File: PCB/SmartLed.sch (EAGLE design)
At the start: 46 parts, among them IC2 DS1307, IC3 MEGA8-P, K1 G5LE, Q1 32.768khz, T1 BC337

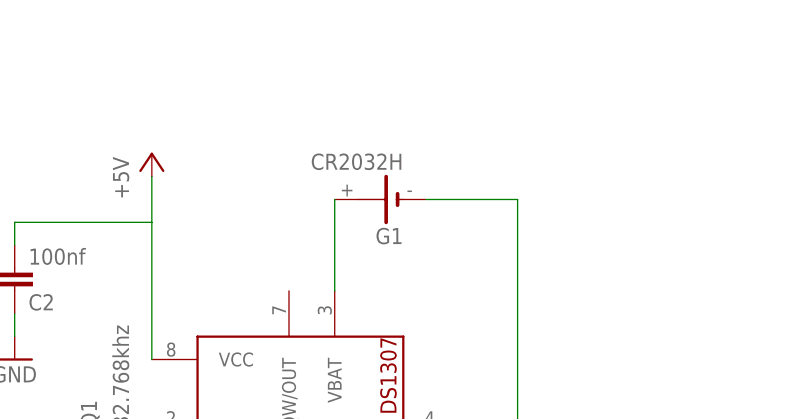
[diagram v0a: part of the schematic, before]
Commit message: Add 100n capacitor beside 3.6v lithium battery & change the battery footprint
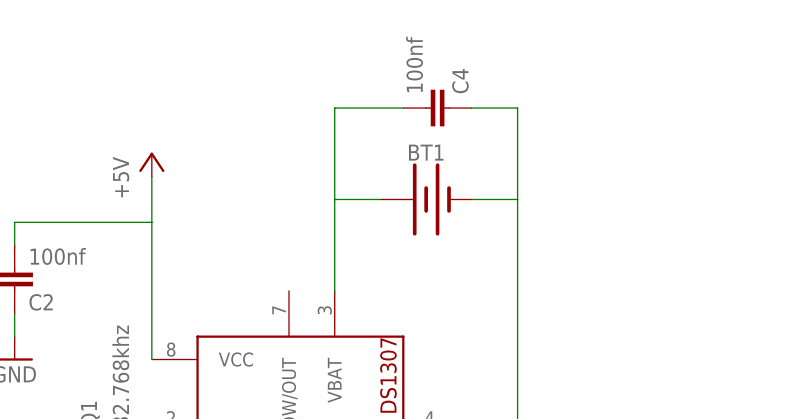
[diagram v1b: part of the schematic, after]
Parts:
- removed G1: CR2032H, battery:CR2032H
- added BT1: (no value), SparkFun-Batteries:BATTERY-20MM_PTH
- added C4: 100nf, rcl:C-EU025-025X050
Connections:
- removed net N$18: G1.+, IC2.VBAT
- new net N$44: BT1.+, C4.2, IC2.VBAT
- net GND: now also BT1.-, C4.1; no longer G1.-
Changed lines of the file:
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@@
 <layer number="112" name="tSilk" color="7" fill="1" visible="no" active="yes"/>
 <layer number="113" name="ReferenceLS" color="7" fill="1" visible="no" active="no"/>
+<layer number="114" name="Badge_Outline" color="7" fill="1" visible="yes" active="yes"/>
+<layer number="115" name="ReferenceISLANDS" color="7" fill="1" visible="yes" active="yes"/>
 <layer number="116" name="Patch_BOT" color="9" fill="4" visible="no" active="yes"/>
 <layer number="118" name="Rect_Pads" color="7" fill="1" visible="no" active="no"/>
@@
 <part name="D1" library="diode" deviceset="1N4148" device="DO35-7"/>
 <part name="IC2" library="adafruit" deviceset="DS1307" device=""/>
-<part name="G1" library="battery" deviceset="CR2032H" device=""/>
 <part name="Q1" library="crystal" deviceset="CRYSTAL" device="HC49U70" value="32.768khz"/>
 <part name="IC3" library="atmel" deviceset="MEGA8-P" device=""/>
@@
 <part name="JP2" library="pinhead" deviceset="PINHD-1X5" device=""/>
 <part name="C1" library="rcl" deviceset="CPOL-EU" device="E2.5-5" value="4.7uf"/>
+<part name="C4" library="rcl" deviceset="C-EU" device="025-025X050" value="100nf"/>
+<part name="BT1" library="SparkFun-Batteries" deviceset="BATTERY" device="-20MM_PTH"/>
 </parts>
 <sheets>
@@
 <instance part="D1" gate="G$1" x="208.28" y="66.04" rot="R90"/>
 <instance part="IC2" gate="G$1" x="208.28" y="157.48" rot="R90"/>
-<instance part="G1" gate="1" x="215.9" y="182.88" rot="R180"/>
 <instance part="Q1" gate="G$1" x="185.42" y="154.94" rot="R90"/>
 <instance part="IC3" gate="G$1" x="66.04" y="88.9"/>
@@
 <instance part="JP2" gate="A" x="101.6" y="116.84"/>
 <instance part="C1" gate="G$1" x="-25.4" y="58.42"/>
+<instance part="C4" gate="G$1" x="223.52" y="193.04" rot="MR90"/>
+<instance part="BT1" gate="G$1" x="220.98" y="182.88"/>
 </instances>
 <busses>
@@
 </segment>
 <segment>
+<pinref part="GND5" gate="1" pin="GND"/>
 <pinref part="IC2" gate="G$1" pin="GND"/>
 <wire x1="223.52" y1="157.48" x2="231.14" y2="157.48" width="0.1524" layer="91"/>
-<pinref part="GND5" gate="1" pin="GND"/>
-<pinref part="G1" gate="1" pin="-"/>
-<wire x1="220.98" y1="182.88" x2="231.14" y2="182.88" width="0.1524" layer="91"/>
+<wire x1="231.14" y1="193.04" x2="231.14" y2="182.88" width="0.1524" layer="91"/>
+<pinref part="C4" gate="G$1" pin="1"/>
 <wire x1="231.14" y1="182.88" x2="231.14" y2="157.48" width="0.1524" layer="91"/>
+<wire x1="226.06" y1="193.04" x2="231.14" y2="193.04" width="0.1524" layer="91"/>
+<pinref part="BT1" gate="G$1" pin="-"/>
+<wire x1="226.06" y1="182.88" x2="231.14" y2="182.88" width="0.1524" layer="91"/>
 </segment>
 <segment>
@@
 </segment>
 </net>
-<net name="N$18" class="0">
-<segment>
-<pinref part="G1" gate="1" pin="+"/>
-<pinref part="IC2" gate="G$1" pin="VBAT"/>
-<wire x1="210.82" y1="182.88" x2="210.82" y2="172.72" width="0.1524" layer="91"/>
-</segment>
-</net>
 <net name="N$21" class="0">
 <segment>
@@
 </segment>
 </net>
+<net name="N$44" class="0">
+<segment>
+<pinref part="C4" gate="G$1" pin="2"/>
+<wire x1="218.44" y1="193.04" x2="210.82" y2="193.04" width="0.1524" layer="91"/>
+<pinref part="IC2" gate="G$1" pin="VBAT"/>
+<wire x1="210.82" y1="193.04" x2="210.82" y2="182.88" width="0.1524" layer="91"/>
+<pinref part="BT1" gate="G$1" pin="+"/>
+<wire x1="210.82" y1="182.88" x2="210.82" y2="172.72" width="0.1524" layer="91"/>
+<wire x1="215.9" y1="182.88" x2="210.82" y2="182.88" width="0.1524" layer="91"/>
+</segment>
+</net>

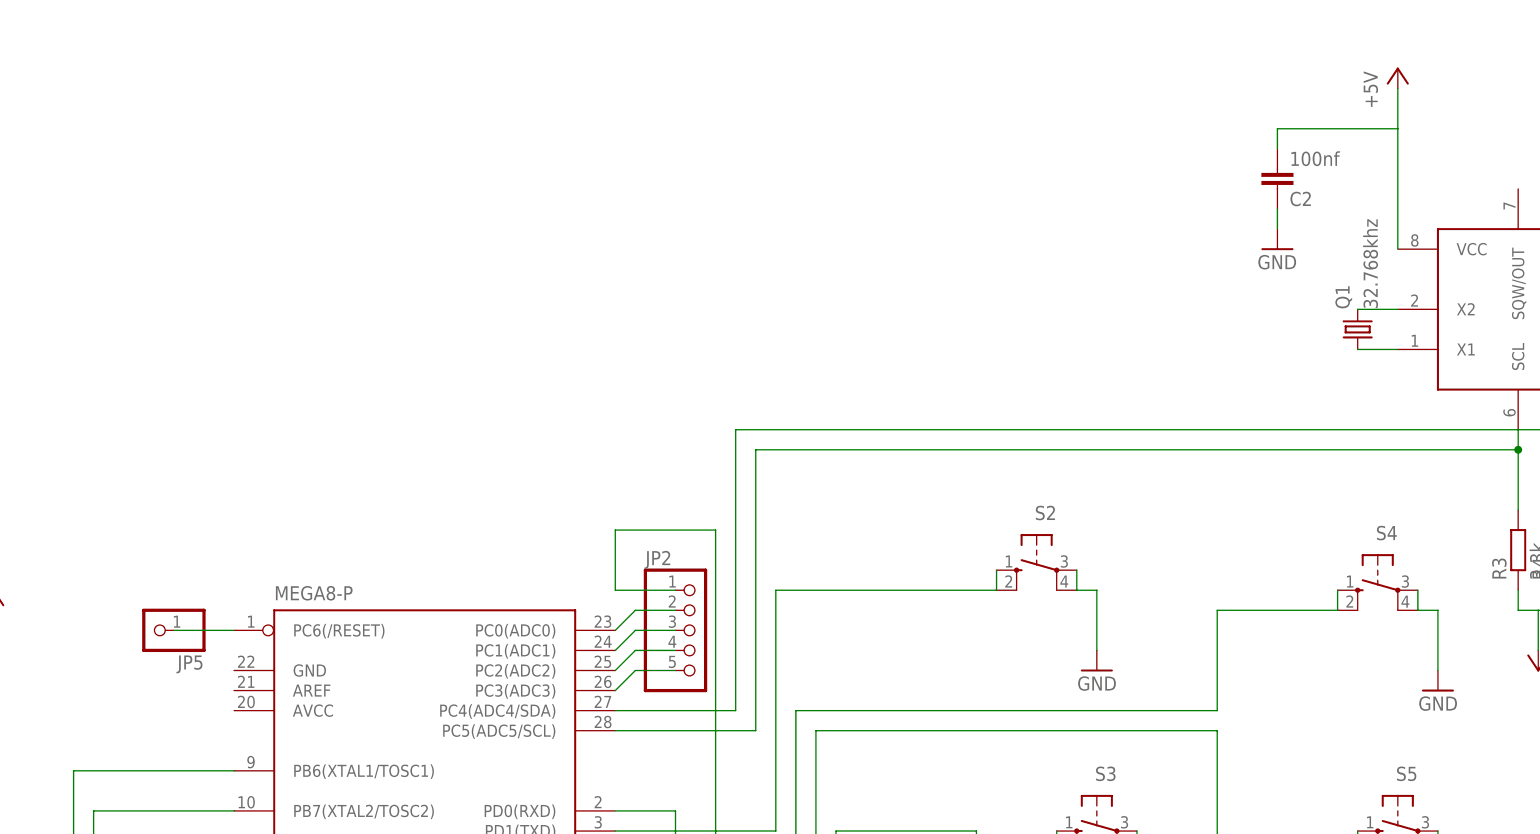
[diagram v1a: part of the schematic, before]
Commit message: Infrared receiver was added & crystal footprint size was corrected
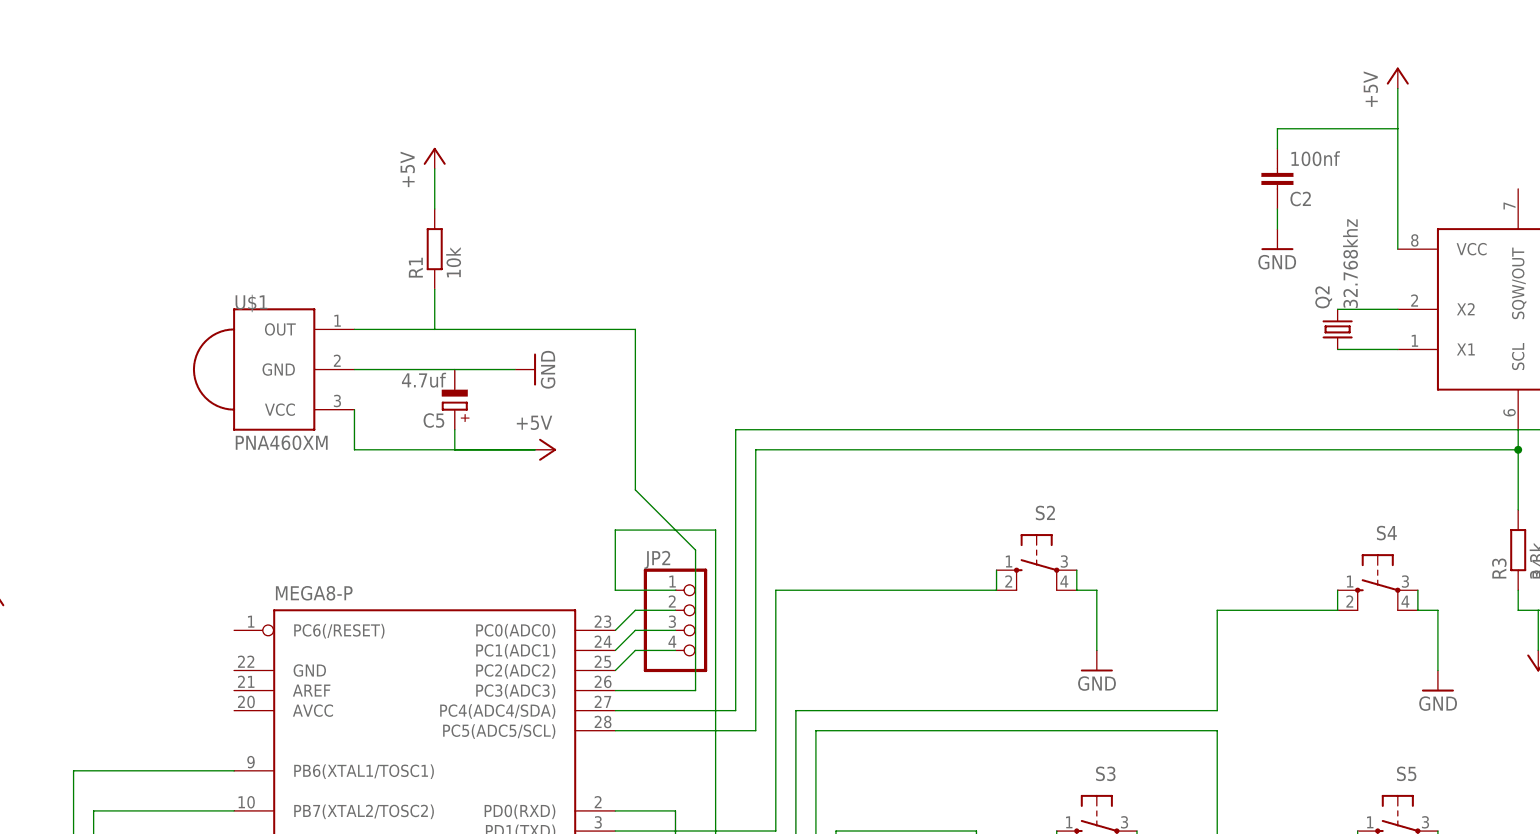
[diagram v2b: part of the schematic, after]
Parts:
- removed JP5: (no value), pinhead:PINHD-1X1
- removed Q1: 32.768khz, crystal:CRYSTALHC49U70
- added C5: 4.7uf, rcl:CPOL-EUE2.5-5
- added Q2: 32.768khz, crystal:CRYSTALTC26V
- added R1: 10k, rcl:R-EU_0207/10
- added U$1: PNA460XM, adafruit:PNA460XM
- JP2: device pinhead:PINHD-1X5 -> pinhead:PINHD-1X4
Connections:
- removed net N$36: IC3.PC3(ADC3), JP2.5
- removed net N$43: IC3.PC6(/RESET), JP5.1
- new net N$46: IC3.PC3(ADC3), R1.1, U$1.OUT
- net +5V: now also C5.+, R1.2, U$1.VCC
- net GND: now also C5.-, U$1.GND
- net N$21: now also Q2.1; no longer Q1.1
- net N$22: now also Q2.2; no longer Q1.2
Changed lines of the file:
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@@
 <part name="D1" library="diode" deviceset="1N4148" device="DO35-7"/>
 <part name="IC2" library="adafruit" deviceset="DS1307" device=""/>
-<part name="Q1" library="crystal" deviceset="CRYSTAL" device="HC49U70" value="32.768khz"/>
 <part name="IC3" library="atmel" deviceset="MEGA8-P" device=""/>
 <part name="B1" library="rectifier" deviceset="RB1A" device=""/>
@@
 <part name="IC4" library="v-reg" deviceset="78XXS" device=""/>
 <part name="GND8" library="supply1" deviceset="GND" device=""/>
-<part name="JP5" library="pinhead" deviceset="PINHD-1X1" device=""/>
 <part name="JP1" library="pinhead" deviceset="PINHD-1X5" device=""/>
-<part name="JP2" library="pinhead" deviceset="PINHD-1X5" device=""/>
 <part name="C1" library="rcl" deviceset="CPOL-EU" device="E2.5-5" value="4.7uf"/>
 <part name="C4" library="rcl" deviceset="C-EU" device="025-025X050" value="100nf"/>
 <part name="BT1" library="SparkFun-Batteries" deviceset="BATTERY" device="-20MM_PTH"/>
+<part name="U$1" library="adafruit" deviceset="PNA460XM" device=""/>
+<part name="C5" library="rcl" deviceset="CPOL-EU" device="E2.5-5" value="4.7uf"/>
+<part name="R1" library="rcl" deviceset="R-EU_" device="0207/10" value="10k"/>
+<part name="GND16" library="supply1" deviceset="GND" device=""/>
+<part name="P+10" library="supply1" deviceset="+5V" device=""/>
+<part name="JP2" library="pinhead" deviceset="PINHD-1X4" device=""/>
+<part name="P+11" library="supply1" deviceset="+5V" device=""/>
+<part name="Q2" library="crystal" deviceset="CRYSTAL" device="TC26V" value="32.768khz"/>
 </parts>
 <sheets>
@@
 <instance part="D1" gate="G$1" x="208.28" y="66.04" rot="R90"/>
 <instance part="IC2" gate="G$1" x="208.28" y="157.48" rot="R90"/>
-<instance part="Q1" gate="G$1" x="185.42" y="154.94" rot="R90"/>
 <instance part="IC3" gate="G$1" x="66.04" y="88.9"/>
 <instance part="B1" gate="1" x="-104.14" y="55.88"/>
@@
 <instance part="IC4" gate="1" x="-5.08" y="111.76"/>
 <instance part="GND8" gate="1" x="175.26" y="165.1"/>
-<instance part="JP5" gate="G$1" x="33.02" y="116.84" rot="R180"/>
 <instance part="JP1" gate="A" x="132.08" y="35.56"/>
-<instance part="JP2" gate="A" x="101.6" y="116.84"/>
 <instance part="C1" gate="G$1" x="-25.4" y="58.42"/>
 <instance part="C4" gate="G$1" x="223.52" y="193.04" rot="MR90"/>
 <instance part="BT1" gate="G$1" x="220.98" y="182.88"/>
+<instance part="U$1" gate="G$1" x="48.26" y="149.86"/>
+<instance part="C5" gate="G$1" x="71.12" y="144.78" rot="R180"/>
+<instance part="R1" gate="G$1" x="68.58" y="165.1" rot="R90"/>
+<instance part="GND16" gate="1" x="81.28" y="149.86" rot="R90"/>
+<instance part="P+10" gate="1" x="83.82" y="139.7" rot="R270"/>
+<instance part="JP2" gate="A" x="101.6" y="116.84"/>
+<instance part="P+11" gate="1" x="68.58" y="177.8"/>
+<instance part="Q2" gate="G$1" x="182.88" y="154.94" rot="R90"/>
 </instances>
 <busses>
@@
 <wire x1="208.28" y1="119.38" x2="208.28" y2="114.3" width="0.1524" layer="91"/>
 </segment>
+<segment>
+<pinref part="C5" gate="G$1" pin="+"/>
+<wire x1="71.12" y1="142.24" x2="71.12" y2="139.7" width="0.1524" layer="91"/>
+<pinref part="P+10" gate="1" pin="+5V"/>
+<wire x1="71.12" y1="139.7" x2="81.28" y2="139.7" width="0.1524" layer="91"/>
+<pinref part="U$1" gate="G$1" pin="VCC"/>
+<wire x1="81.28" y1="139.7" x2="58.42" y2="139.7" width="0.1524" layer="91"/>
+<wire x1="58.42" y1="139.7" x2="58.42" y2="144.78" width="0.1524" layer="91"/>
+</segment>
+<segment>
+<pinref part="P+11" gate="1" pin="+5V"/>
+<pinref part="R1" gate="G$1" pin="2"/>
+<wire x1="68.58" y1="175.26" x2="68.58" y2="170.18" width="0.1524" layer="91"/>
+</segment>
 </net>
 <net name="GND" class="0">
@@
 <wire x1="175.26" y1="170.18" x2="175.26" y2="167.64" width="0.1524" layer="91"/>
 </segment>
+<segment>
+<pinref part="C5" gate="G$1" pin="-"/>
+<pinref part="U$1" gate="G$1" pin="GND"/>
+<wire x1="71.12" y1="149.86" x2="58.42" y2="149.86" width="0.1524" layer="91"/>
+<pinref part="GND16" gate="1" pin="GND"/>
+<wire x1="71.12" y1="149.86" x2="78.74" y2="149.86" width="0.1524" layer="91"/>
+</segment>
 </net>
 <net name="N$12" class="0">
@@
 <net name="N$21" class="0">
 <segment>
-<pinref part="Q1" gate="G$1" pin="1"/>
 <pinref part="IC2" gate="G$1" pin="X1"/>
-<wire x1="185.42" y1="152.4" x2="190.5" y2="152.4" width="0.1524" layer="91"/>
+<wire x1="182.88" y1="152.4" x2="190.5" y2="152.4" width="0.1524" layer="91"/>
+<pinref part="Q2" gate="G$1" pin="1"/>
 </segment>
 </net>
 <net name="N$22" class="0">
 <segment>
-<pinref part="Q1" gate="G$1" pin="2"/>
 <pinref part="IC2" gate="G$1" pin="X2"/>
-<wire x1="185.42" y1="157.48" x2="190.5" y2="157.48" width="0.1524" layer="91"/>
+<wire x1="182.88" y1="157.48" x2="190.5" y2="157.48" width="0.1524" layer="91"/>
+<pinref part="Q2" gate="G$1" pin="2"/>
 </segment>
 </net>
@@
 </segment>
 </net>
-<net name="N$36" class="0">
-<segment>
-<wire x1="93.98" y1="111.76" x2="99.06" y2="111.76" width="0.1524" layer="91"/>
-<pinref part="IC3" gate="G$1" pin="PC3(ADC3)"/>
-<wire x1="93.98" y1="111.76" x2="91.44" y2="109.22" width="0.1524" layer="91"/>
-<pinref part="JP2" gate="A" pin="5"/>
-</segment>
-</net>
-<net name="N$38" class="0">
-<segment>
-<wire x1="93.98" y1="116.84" x2="99.06" y2="116.84" width="0.1524" layer="91"/>
-<pinref part="IC3" gate="G$1" pin="PC1(ADC1)"/>
-<wire x1="93.98" y1="116.84" x2="91.44" y2="114.3" width="0.1524" layer="91"/>
-<pinref part="JP2" gate="A" pin="3"/>
-</segment>
-</net>
-<net name="N$30" class="0">
-<segment>
-<wire x1="99.06" y1="119.38" x2="93.98" y2="119.38" width="0.1524" layer="91"/>
-<pinref part="IC3" gate="G$1" pin="PC0(ADC0)"/>
-<wire x1="93.98" y1="119.38" x2="91.44" y2="116.84" width="0.1524" layer="91"/>
-<pinref part="JP2" gate="A" pin="2"/>
-</segment>
-</net>
-<net name="N$34" class="0">
-<segment>
-<wire x1="99.06" y1="114.3" x2="93.98" y2="114.3" width="0.1524" layer="91"/>
-<pinref part="IC3" gate="G$1" pin="PC2(ADC2)"/>
-<wire x1="93.98" y1="114.3" x2="91.44" y2="111.76" width="0.1524" layer="91"/>
-<pinref part="JP2" gate="A" pin="4"/>
-</segment>
-</net>
 <net name="N$35" class="0">
 <segment>
@@
 <wire x1="129.54" y1="35.56" x2="124.46" y2="35.56" width="0.1524" layer="91"/>
 <wire x1="124.46" y1="35.56" x2="124.46" y2="81.28" width="0.1524" layer="91"/>
-</segment>
-</net>
-<net name="N$43" class="0">
-<segment>
-<pinref part="JP5" gate="G$1" pin="1"/>
-<pinref part="IC3" gate="G$1" pin="PC6(/RESET)"/>
-<wire x1="35.56" y1="116.84" x2="43.18" y2="116.84" width="0.1524" layer="91"/>
 </segment>
 </net>
@@
 <wire x1="91.44" y1="129.54" x2="91.44" y2="121.92" width="0.1524" layer="91"/>
 <pinref part="JP2" gate="A" pin="1"/>
-<wire x1="91.44" y1="121.92" x2="99.06" y2="121.92" width="0.1524" layer="91"/>
+<wire x1="99.06" y1="121.92" x2="91.44" y2="121.92" width="0.1524" layer="91"/>
 </segment>
 </net>
@@
 </segment>
 </net>
+<net name="N$46" class="0">
+<segment>
+<wire x1="93.98" y1="154.94" x2="93.98" y2="134.62" width="0.1524" layer="91"/>
+<wire x1="93.98" y1="134.62" x2="101.6" y2="127" width="0.1524" layer="91"/>
+<wire x1="101.6" y1="127" x2="101.6" y2="109.22" width="0.1524" layer="91"/>
+<pinref part="IC3" gate="G$1" pin="PC3(ADC3)"/>
+<wire x1="101.6" y1="109.22" x2="91.44" y2="109.22" width="0.1524" layer="91"/>
+<pinref part="U$1" gate="G$1" pin="OUT"/>
+<wire x1="58.42" y1="154.94" x2="68.58" y2="154.94" width="0.1524" layer="91"/>
+<pinref part="R1" gate="G$1" pin="1"/>
+<wire x1="68.58" y1="154.94" x2="93.98" y2="154.94" width="0.1524" layer="91"/>
+<wire x1="68.58" y1="154.94" x2="68.58" y2="160.02" width="0.1524" layer="91"/>
+</segment>
+</net>
+<net name="N$18" class="0">
+<segment>
+<pinref part="JP2" gate="A" pin="2"/>
+<pinref part="IC3" gate="G$1" pin="PC0(ADC0)"/>
+<wire x1="99.06" y1="119.38" x2="93.98" y2="119.38" width="0.1524" layer="91"/>
+<wire x1="93.98" y1="119.38" x2="91.44" y2="116.84" width="0.1524" layer="91"/>
+</segment>
+</net>
+<net name="N$30" class="0">
+<segment>
+<pinref part="JP2" gate="A" pin="3"/>
+<pinref part="IC3" gate="G$1" pin="PC1(ADC1)"/>
+<wire x1="99.06" y1="116.84" x2="93.98" y2="116.84" width="0.1524" layer="91"/>
+<wire x1="93.98" y1="116.84" x2="91.44" y2="114.3" width="0.1524" layer="91"/>
+</segment>
+</net>
+<net name="N$34" class="0">
+<segment>
+<pinref part="JP2" gate="A" pin="4"/>
+<pinref part="IC3" gate="G$1" pin="PC2(ADC2)"/>
+<wire x1="99.06" y1="114.3" x2="93.98" y2="114.3" width="0.1524" layer="91"/>
+<wire x1="93.98" y1="114.3" x2="91.44" y2="111.76" width="0.1524" layer="91"/>
+</segment>
+</net>
